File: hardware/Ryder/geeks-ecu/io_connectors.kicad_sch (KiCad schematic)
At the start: 65 parts, among them J401 JST XH, J402 JST XH, J403 Grove, J404 JST XH, J405 JST XH, J406 3x6 2.54mm, J407 RJ45, J408 JST XH, J409 JST XH, Q401 2N7002, Q402 2N7002

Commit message: asdf
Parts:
- removed C416: 1uF, Capacitor_SMD:C_0603_1608Metric, symbol Device:C
- removed C420: 0.1uF, Capacitor_SMD:C_0603_1608Metric, symbol Device:C
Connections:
- net VBAT: no longer names the net of J405.1 (Pin_1)
- no-connect marks 4 -> 5
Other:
- moved on the sheet: C417, C421

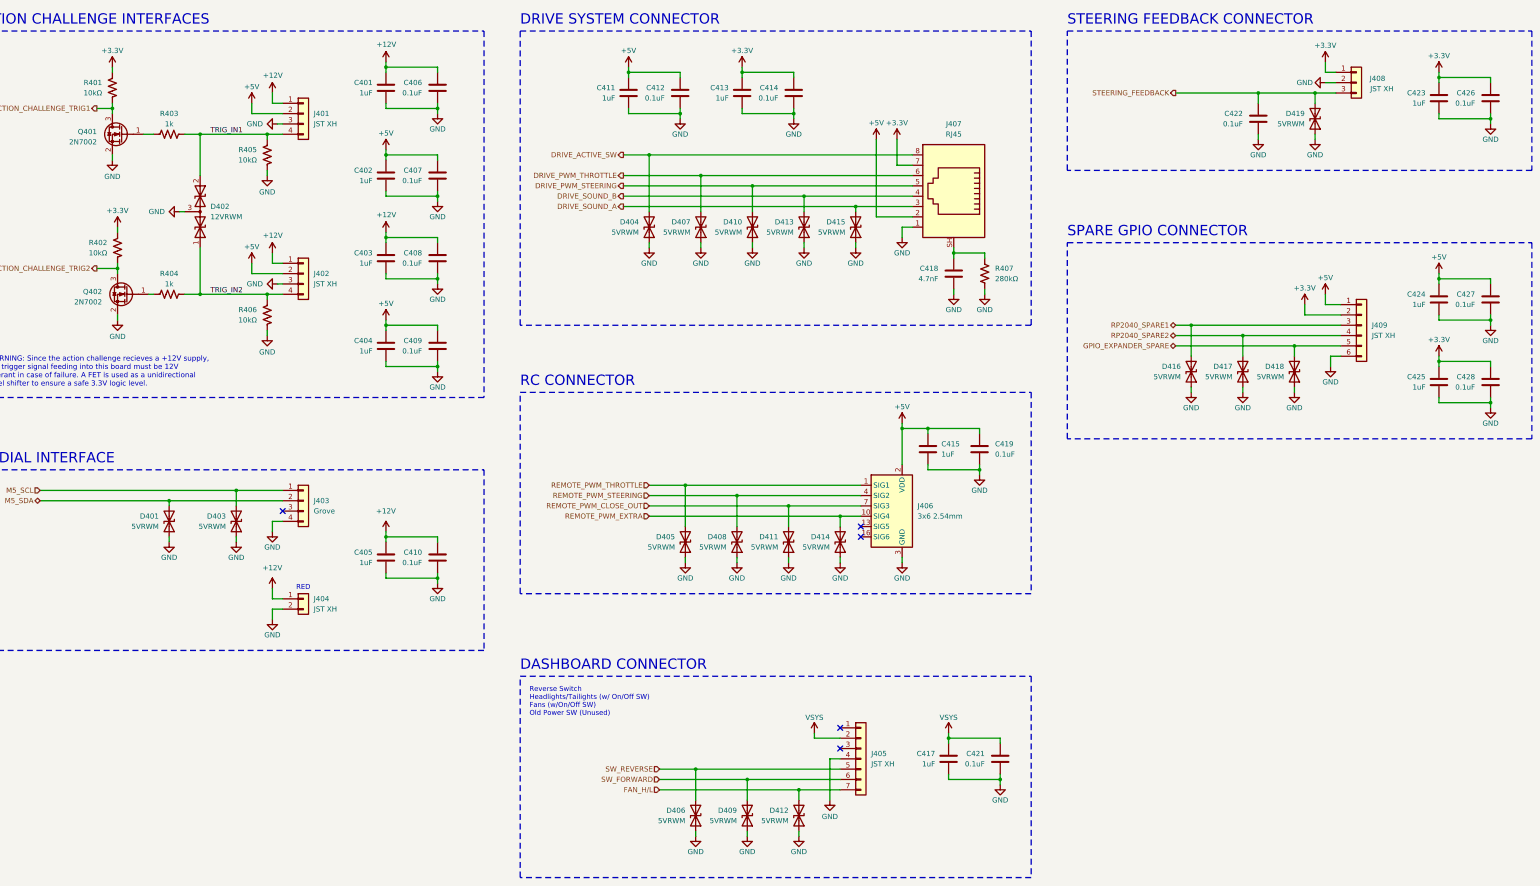
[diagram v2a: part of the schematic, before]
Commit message: Ryder ECU Cleanup
Still need to work on high current traces
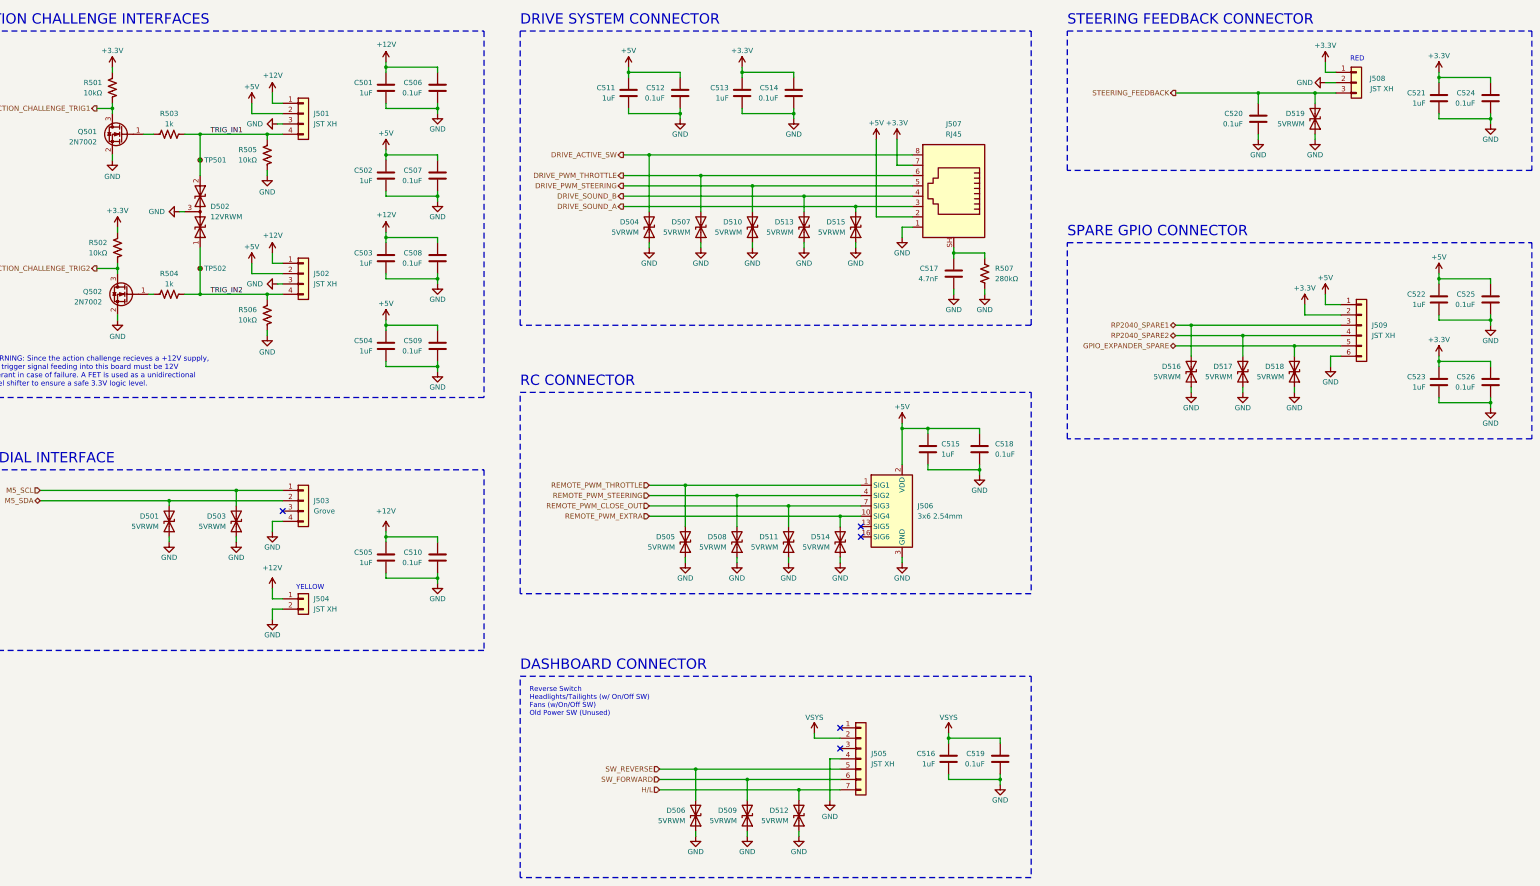
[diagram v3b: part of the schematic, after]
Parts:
- removed J404: JST XH, geeks-ecu-footprints:JST_XH_B2B-XH-AM_1x02_P2.50mm_Vertical, symbol Connector_Generic:Conn_01x02
- added J504: JST XH, geeks-ecu-footprints:JST_XH_B2B-XH-AM_1x02_P2.50mm_Vertical, symbol Connector_Generic:Conn_01x02
- added TP501, TP502: TestPoint_Small, geeks-ecu-footprints:TestPoint_Pad_D1.0mm, symbol Connector:TestPoint_Small
- C501: renamed from C401; footprint Capacitor_SMD:C_0603_1608Metric -> geeks-ecu-footprints:C_0603_1608Metric
- C502: renamed from C402; footprint Capacitor_SMD:C_0603_1608Metric -> geeks-ecu-footprints:C_0603_1608Metric
- C503: renamed from C403; footprint Capacitor_SMD:C_0603_1608Metric -> geeks-ecu-footprints:C_0603_1608Metric
- C504: renamed from C404; footprint Capacitor_SMD:C_0603_1608Metric -> geeks-ecu-footprints:C_0603_1608Metric
- C505: renamed from C405; footprint Capacitor_SMD:C_0603_1608Metric -> geeks-ecu-footprints:C_0603_1608Metric
- C506: renamed from C406; footprint Capacitor_SMD:C_0603_1608Metric -> geeks-ecu-footprints:C_0603_1608Metric
- C507: renamed from C407; footprint Capacitor_SMD:C_0603_1608Metric -> geeks-ecu-footprints:C_0603_1608Metric
- C508: renamed from C408; footprint Capacitor_SMD:C_0603_1608Metric -> geeks-ecu-footprints:C_0603_1608Metric
- C509: renamed from C409; footprint Capacitor_SMD:C_0603_1608Metric -> geeks-ecu-footprints:C_0603_1608Metric
- C510: renamed from C410; footprint Capacitor_SMD:C_0603_1608Metric -> geeks-ecu-footprints:C_0603_1608Metric
- C511: renamed from C411; footprint Capacitor_SMD:C_0603_1608Metric -> geeks-ecu-footprints:C_0603_1608Metric
- C512: renamed from C412; footprint Capacitor_SMD:C_0603_1608Metric -> geeks-ecu-footprints:C_0603_1608Metric
- C513: renamed from C413; footprint Capacitor_SMD:C_0603_1608Metric -> geeks-ecu-footprints:C_0603_1608Metric
- C514: renamed from C414; footprint Capacitor_SMD:C_0603_1608Metric -> geeks-ecu-footprints:C_0603_1608Metric
- C515: renamed from C415; footprint Capacitor_SMD:C_0603_1608Metric -> geeks-ecu-footprints:C_0603_1608Metric
- C516: renamed from C417; footprint Capacitor_SMD:C_0603_1608Metric -> geeks-ecu-footprints:C_0603_1608Metric
- C517: renamed from C418; footprint Capacitor_SMD:C_0805_2012Metric -> geeks-ecu-footprints:C_0805_2012Metric
- C518: renamed from C419; footprint Capacitor_SMD:C_0603_1608Metric -> geeks-ecu-footprints:C_0603_1608Metric
- C519: renamed from C421; footprint Capacitor_SMD:C_0603_1608Metric -> geeks-ecu-footprints:C_0603_1608Metric
- C520: renamed from C422; footprint Capacitor_SMD:C_0603_1608Metric -> geeks-ecu-footprints:C_0603_1608Metric
- C521: renamed from C423; footprint Capacitor_SMD:C_0603_1608Metric -> geeks-ecu-footprints:C_0603_1608Metric
- C522: renamed from C424; footprint Capacitor_SMD:C_0603_1608Metric -> geeks-ecu-footprints:C_0603_1608Metric
- C523: renamed from C425; footprint Capacitor_SMD:C_0603_1608Metric -> geeks-ecu-footprints:C_0603_1608Metric
- C524: renamed from C426; footprint Capacitor_SMD:C_0603_1608Metric -> geeks-ecu-footprints:C_0603_1608Metric
- C525: renamed from C427; footprint Capacitor_SMD:C_0603_1608Metric -> geeks-ecu-footprints:C_0603_1608Metric
- C526: renamed from C428; footprint Capacitor_SMD:C_0603_1608Metric -> geeks-ecu-footprints:C_0603_1608Metric
- D501: renamed from D401; footprint Diode_SMD:D_SOD-882 -> geeks-ecu-footprints:D_SOD-882
- D502: renamed from D402; footprint Package_TO_SOT_SMD:SOT-23 -> geeks-ecu-footprints:SOT-23
- D503: renamed from D403; footprint Diode_SMD:D_SOD-882 -> geeks-ecu-footprints:D_SOD-882
- D504: renamed from D404; footprint Diode_SMD:D_SOD-882 -> geeks-ecu-footprints:D_SOD-882
- D505: renamed from D405; footprint Diode_SMD:D_SOD-882 -> geeks-ecu-footprints:D_SOD-882
- D506: renamed from D406; footprint Diode_SMD:D_SOD-882 -> geeks-ecu-footprints:D_SOD-882
- D507: renamed from D407; footprint Diode_SMD:D_SOD-882 -> geeks-ecu-footprints:D_SOD-882
- D508: renamed from D408; footprint Diode_SMD:D_SOD-882 -> geeks-ecu-footprints:D_SOD-882
- D509: renamed from D409; footprint Diode_SMD:D_SOD-882 -> geeks-ecu-footprints:D_SOD-882
- D510: renamed from D410; footprint Diode_SMD:D_SOD-882 -> geeks-ecu-footprints:D_SOD-882
- D511: renamed from D411; footprint Diode_SMD:D_SOD-882 -> geeks-ecu-footprints:D_SOD-882
- D512: renamed from D412; footprint Diode_SMD:D_SOD-882 -> geeks-ecu-footprints:D_SOD-882
- D513: renamed from D413; footprint Diode_SMD:D_SOD-882 -> geeks-ecu-footprints:D_SOD-882
- D514: renamed from D414; footprint Diode_SMD:D_SOD-882 -> geeks-ecu-footprints:D_SOD-882
- D515: renamed from D415; footprint Diode_SMD:D_SOD-882 -> geeks-ecu-footprints:D_SOD-882
- D516: renamed from D416; footprint Diode_SMD:D_SOD-882 -> geeks-ecu-footprints:D_SOD-882
- D517: renamed from D417; footprint Diode_SMD:D_SOD-882 -> geeks-ecu-footprints:D_SOD-882
- D518: renamed from D418; footprint Diode_SMD:D_SOD-882 -> geeks-ecu-footprints:D_SOD-882
- D519: renamed from D419; footprint Diode_SMD:D_SOD-882 -> geeks-ecu-footprints:D_SOD-882
- J505: renamed from J405; MPN (none) -> C161874
- J508: renamed from J408; MPN C161870 -> (none); now left out of the parts list
- Q501: renamed from Q401; footprint Package_TO_SOT_SMD:SOT-23 -> geeks-ecu-footprints:SOT-23
- Q502: renamed from Q402; footprint Package_TO_SOT_SMD:SOT-23 -> geeks-ecu-footprints:SOT-23
- R501: renamed from R401; footprint Resistor_SMD:R_0603_1608Metric -> geeks-ecu-footprints:R_0603_1608Metric
- R502: renamed from R402; footprint Resistor_SMD:R_0603_1608Metric -> geeks-ecu-footprints:R_0603_1608Metric
- R503: renamed from R403; footprint Resistor_SMD:R_0603_1608Metric -> geeks-ecu-footprints:R_0603_1608Metric
- R504: renamed from R404; footprint Resistor_SMD:R_0603_1608Metric -> geeks-ecu-footprints:R_0603_1608Metric
- R505: renamed from R405; footprint Resistor_SMD:R_0603_1608Metric -> geeks-ecu-footprints:R_0603_1608Metric
- R506: renamed from R406; footprint Resistor_SMD:R_0603_1608Metric -> geeks-ecu-footprints:R_0603_1608Metric
- R507: renamed from R407; footprint Resistor_SMD:R_0603_1608Metric -> geeks-ecu-footprints:R_0603_1608Metric
- renumbered J401 to J501, J402 to J502, J403 to J503, J406 to J506, J407 to J507, J409 to J509
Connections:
- net +12V: now also J504.1 (Pin_1)
- net GND: now also J504.2 (Pin_2)
- net TRIG_IN1: now also TP501.1
- net TRIG_IN2: now also TP502.1
- net FAN_H/L renamed H/L
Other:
- note added: "YELLOW"

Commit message: Finalize Ryder ECU
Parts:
- J506, J507: now left out of the parts list
- Q501, Q502: MPN C8545 -> C22446827

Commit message: Final Ryder ECU Design Files
All done!
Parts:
- R503, R504: value 1k -> 1kΩ; MPN C11702 -> C21190
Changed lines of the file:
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@@
 	)
 	(symbol
+		(lib_id "Device:R_US")
+		(at 72.39 59.69 90)
+		(unit 1)
+		(body_style 1)
+		(exclude_from_sim no)
+		(in_bom yes)
+		(on_board yes)
+		(in_pos_files yes)
+		(dnp no)
+		(property "Reference" "R503"
+			(at 72.39 54.61 90)
+			(show_name no)
+			(do_not_autoplace no)
+			(effects
+				(font
+					(size 1.27 1.27)
+				)
+			)
+		)
+		(property "Value" "1kΩ"
+			(at 72.39 57.15 90)
+			(show_name no)
+			(do_not_autoplace no)
+			(effects
+				(font
+					(size 1.27 1.27)
+				)
+			)
+		)
+		(property "Footprint" "geeks-ecu-footprints:R_0603_1608Metric"
+			(at 72.644 58.674 90)
+			(hide yes)
+			(show_name no)
+			(do_not_autoplace no)
+			(effects
+				(font
+					(size 1.27 1.27)
+				)
+			)
+		)
+		(property "Datasheet" "https://www.lcsc.com/datasheet/C21190.pdf?spm=wm.sxq.inf.ggs&lcsc_vid=ElldVlQDQlVXA1BeQgUMVlBQEVdaUVcARVFWXlFXRlcxVlNRQFJaVlFVR1hZVTsOAxUeFF5JWBYZEEoKFBINSQcJGk4eFQsCAgIaSgADAwAHC0slRFBfUVJRWQkaCgg%3D"
+			(at 72.39 59.69 0)
+			(hide yes)
+			(show_name no)
+			(do_not_autoplace no)
+			(effects
+				(font
+					(size 1.27 1.27)
+				)
+			)
+		)
+		(property "Description" "RES 1kΩ ±1% 100mW 0603"
+			(at 72.39 59.69 0)
+			(hide yes)
+			(show_name no)
+			(do_not_autoplace no)
+			(effects
+				(font
+					(size 1.27 1.27)
+				)
+			)
+		)
+		(property "MPN" "C21190"
+			(at 72.39 59.69 0)
+			(hide yes)
+			(show_name no)
+			(do_not_autoplace no)
+			(effects
+				(font
+					(size 1.27 1.27)
+				)
+			)
+		)
+		(property "MPN`" ""
+			(at 72.39 59.69 90)
+			(hide yes)
+			(show_name no)
+			(do_not_autoplace no)
+			(effects
+				(font
+					(size 1.27 1.27)
+				)
+			)
+		)
+		(pin "2"
+		)
+		(pin "1"
+		)
+		(instances
+			(project "geeks-ecu"
+				(path "/f2eba3ec-213e-460f-84b8-405fb1bcb4da/75652050-2907-4906-b92b-af5ffa0f2373"
+					(reference "R503")
+					(unit 1)
+				)
+			)
+		)
+	)
+	(symbol
 		(lib_id "power:+3.3V")
 		(at 384.81 44.45 0)
@@
 		(in_bom no)
 		(on_board yes)
-		(in_pos_files yes)
+		(in_pos_files no)
 		(dnp no)
 		(property "Reference" "J503"
@@
 	)
 	(symbol
-		(lib_id "Device:R_US")
-		(at 72.39 59.69 90)
-		(unit 1)
-		(body_style 1)
-		(exclude_from_sim no)
-		(in_bom yes)
-		(on_board yes)
-		(in_pos_files yes)
-		(dnp no)
-		(fields_autoplaced yes)
-		(property "Reference" "R503"
-			(at 72.39 54.61 90)
-			(show_name no)
-			(do_not_autoplace no)
-			(effects
-				(font
-					(size 1.27 1.27)
-				)
-			)
-		)
-		(property "Value" "1k"
-			(at 72.39 57.15 90)
-			(show_name no)
-			(do_not_autoplace no)
-			(effects
-				(font
-					(size 1.27 1.27)
-				)
-			)
-		)
-		(property "Footprint" "geeks-ecu-footprints:R_0603_1608Metric"
-			(at 72.644 58.674 90)
-			(hide yes)
-			(show_name no)
-			(do_not_autoplace no)
-			(effects
-				(font
-					(size 1.27 1.27)
-				)
-			)
-		)
-		(property "Datasheet" ""
-			(at 72.39 59.69 0)
-			(hide yes)
-			(show_name no)
-			(do_not_autoplace no)
-			(effects
-				(font
-					(size 1.27 1.27)
-				)
-			)
-		)
-		(property "Description" "RES 1kΩ ±1% 62.5mW 0402"
-			(at 72.39 59.69 0)
-			(hide yes)
-			(show_name no)
-			(do_not_autoplace no)
-			(effects
-				(font
-					(size 1.27 1.27)
-				)
-			)
-		)
-		(property "MPN" "C11702"
-			(at 72.39 59.69 90)
-			(hide yes)
-			(show_name no)
-			(do_not_autoplace no)
-			(effects
-				(font
-					(size 1.27 1.27)
-				)
-			)
-		)
-		(property "MPN`" ""
-			(at 72.39 59.69 90)
-			(hide yes)
-			(show_name no)
-			(do_not_autoplace no)
-			(effects
-				(font
-					(size 1.27 1.27)
-				)
-			)
-		)
-		(pin "1"
-		)
-		(pin "2"
-		)
-		(instances
-			(project "geeks-ecu"
-				(path "/f2eba3ec-213e-460f-84b8-405fb1bcb4da/75652050-2907-4906-b92b-af5ffa0f2373"
-					(reference "R503")
-					(unit 1)
-				)
-			)
-		)
-	)
-	(symbol
 		(lib_id "power:GND")
 		(at 74.93 78.74 270)
@@
 	(symbol
 		(lib_id "Device:R_US")
-		(at 72.39 99.06 90)
-		(unit 1)
-		(body_style 1)
-		(exclude_from_sim no)
-		(in_bom yes)
-		(on_board yes)
-		(in_pos_files yes)
-		(dnp no)
-		(fields_autoplaced yes)
-		(property "Reference" "R504"
-			(at 72.39 93.98 90)
-			(show_name no)
-			(do_not_autoplace no)
-			(effects
-				(font
-					(size 1.27 1.27)
-				)
-			)
-		)
-		(property "Value" "1k"
-			(at 72.39 96.52 90)
-			(show_name no)
-			(do_not_autoplace no)
-			(effects
-				(font
-					(size 1.27 1.27)
-				)
-			)
-		)
-		(property "Footprint" "geeks-ecu-footprints:R_0603_1608Metric"
-			(at 72.644 98.044 90)
-			(hide yes)
-			(show_name no)
-			(do_not_autoplace no)
-			(effects
-				(font
-					(size 1.27 1.27)
-				)
-			)
-		)
-		(property "Datasheet" ""
-			(at 72.39 99.06 0)
-			(hide yes)
-			(show_name no)
-			(do_not_autoplace no)
-			(effects
-				(font
-					(size 1.27 1.27)
-				)
-			)
-		)
-		(property "Description" "RES 1kΩ ±1% 62.5mW 0402"
-			(at 72.39 99.06 0)
-			(hide yes)
-			(show_name no)
-			(do_not_autoplace no)
-			(effects
-				(font
-					(size 1.27 1.27)
-				)
-			)
-		)
-		(property "MPN" "C11702"
-			(at 72.39 99.06 90)
-			(hide yes)
-			(show_name no)
-			(do_not_autoplace no)
-			(effects
-				(font
-					(size 1.27 1.27)
-				)
-			)
-		)
-		(property "MPN`" ""
-			(at 72.39 99.06 90)
-			(hide yes)
-			(show_name no)
-			(do_not_autoplace no)
-			(effects
-				(font
-					(size 1.27 1.27)
-				)
-			)
-		)
-		(pin "1"
-		)
-		(pin "2"
-		)
-		(instances
-			(project "geeks-ecu"
-				(path "/f2eba3ec-213e-460f-84b8-405fb1bcb4da/75652050-2907-4906-b92b-af5ffa0f2373"
-					(reference "R504")
-					(unit 1)
-				)
-			)
-		)
-	)
-	(symbol
-		(lib_id "Device:R_US")
 		(at 96.52 104.14 0)
 		(mirror y)
@@
 					(unit 1)
 				)
+			)
+		)
+	)
+	(symbol
+		(lib_id "Device:R_US")
+		(at 72.39 99.06 90)
+		(unit 1)
+		(body_style 1)
+		(exclude_from_sim no)
+		(in_bom yes)
+		(on_board yes)
+		(in_pos_files yes)
+		(dnp no)
+		(property "Reference" "R504"
+			(at 72.39 93.98 90)
+			(show_name no)
+			(do_not_autoplace no)
+			(effects
+				(font
+					(size 1.27 1.27)
+				)
+			)
+		)
+		(property "Value" "1kΩ"
+			(at 72.39 96.52 90)
+			(show_name no)
+			(do_not_autoplace no)
+			(effects
+				(font
+					(size 1.27 1.27)
+				)
+			)
+		)
+		(property "Footprint" "geeks-ecu-footprints:R_0603_1608Metric"
+			(at 72.644 98.044 90)
+			(hide yes)
+			(show_name no)
+			(do_not_autoplace no)
+			(effects
+				(font
+					(size 1.27 1.27)
+				)
+			)
+		)
+		(property "Datasheet" "https://www.lcsc.com/datasheet/C21190.pdf?spm=wm.sxq.inf.ggs&lcsc_vid=ElldVlQDQlVXA1BeQgUMVlBQEVdaUVcARVFWXlFXRlcxVlNRQFJaVlFVR1hZVTsOAxUeFF5JWBYZEEoKFBINSQcJGk4eFQsCAgIaSgADAwAHC0slRFBfUVJRWQkaCgg%3D"
+			(at 72.39 99.06 0)
+			(hide yes)
+			(show_name no)
+			(do_not_autoplace no)
+			(effects
+				(font
+					(size 1.27 1.27)
+				)
+			)
+		)
+		(property "Description" "RES 1kΩ ±1% 100mW 0603"
+			(at 72.39 99.06 0)
+			(hide yes)
+			(show_name no)
+			(do_not_autoplace no)
+			(effects
+				(font
+					(size 1.27 1.27)
+				)
+			)
+		)
+		(property "MPN" "C21190"
+			(at 72.39 99.06 0)
+			(hide yes)
+			(show_name no)
+			(do_not_autoplace no)
+			(effects
+				(font
+					(size 1.27 1.27)
+				)
+			)
+		)
+		(property "MPN`" ""
+			(at 72.39 99.06 90)
+			(hide yes)
+			(show_name no)
+			(do_not_autoplace no)
+			(effects
+				(font
+					(size 1.27 1.27)
+				)
+			)
+		)
+		(pin "2"
+		)
+		(pin "1"
+		)
+		(instances
+			(project "geeks-ecu"
+				(path "/f2eba3ec-213e-460f-84b8-405fb1bcb4da/75652050-2907-4906-b92b-af5ffa0f2373"
+					(reference "R504")
+					(unit 1)
+				)
